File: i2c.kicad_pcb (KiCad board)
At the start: 2 copper layers, 2 parts

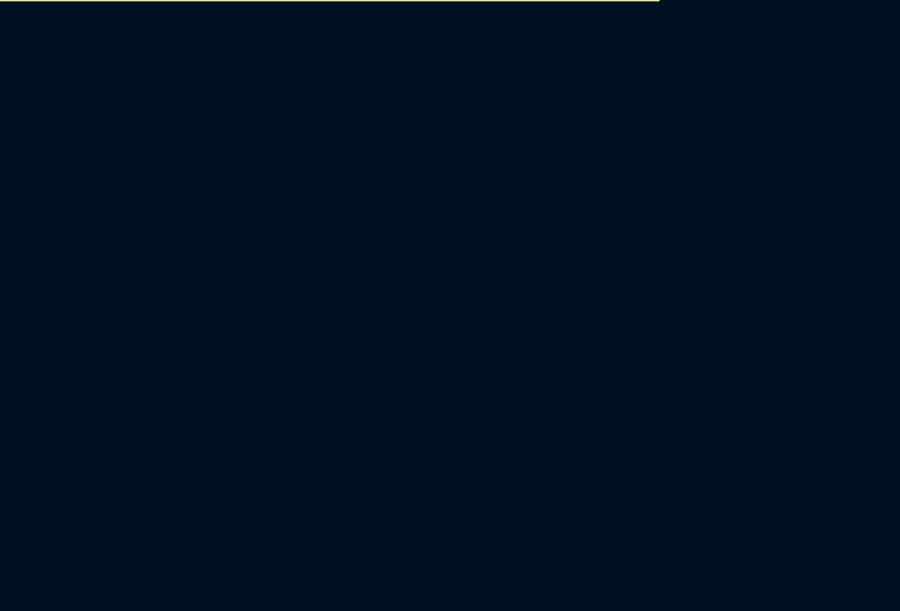
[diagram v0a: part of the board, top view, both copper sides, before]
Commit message: se agregaron 2 componenetes nuevos y se ajusto el pcb, falta agregar footprints
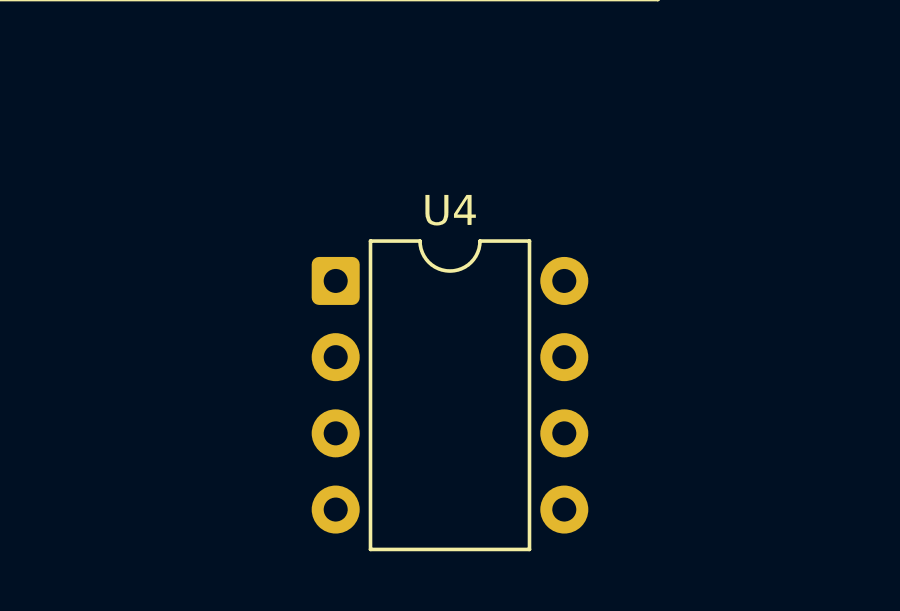
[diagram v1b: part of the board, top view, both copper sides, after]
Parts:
- added U4: ADG417BN, Package_DIP:DIP-8_W7.62mm, F.Cu at (130.4, 77.4)
